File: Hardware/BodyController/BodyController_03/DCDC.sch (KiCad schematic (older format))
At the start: 58 parts, among them Q12 BUK9Y3R0-40E,115, Q13 BUK9Y3R0-40E,115, Q14 BUK9Y3R0-40E,115, Q16 2N7002, Q6 NX1029X,115, Q7 NX1029X,115, U21 LM2903QDRQ1, U25 UCC27511A-Q1, U27 INA21x, U28 OPA320-Q1

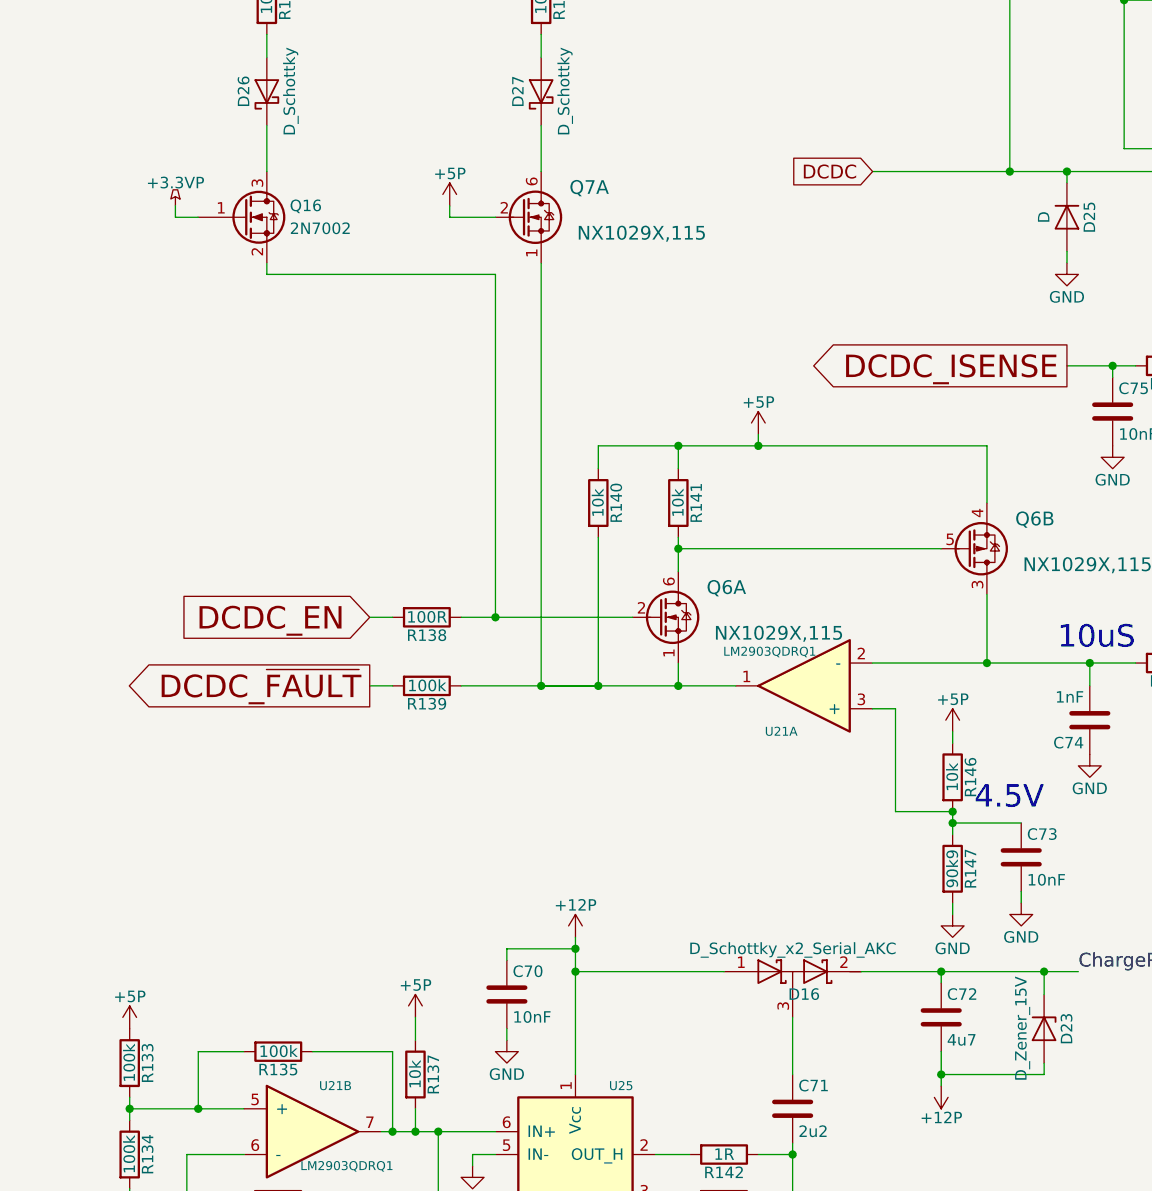
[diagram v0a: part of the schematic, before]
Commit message: Updated layout, cleaned up directory, and modified BOM
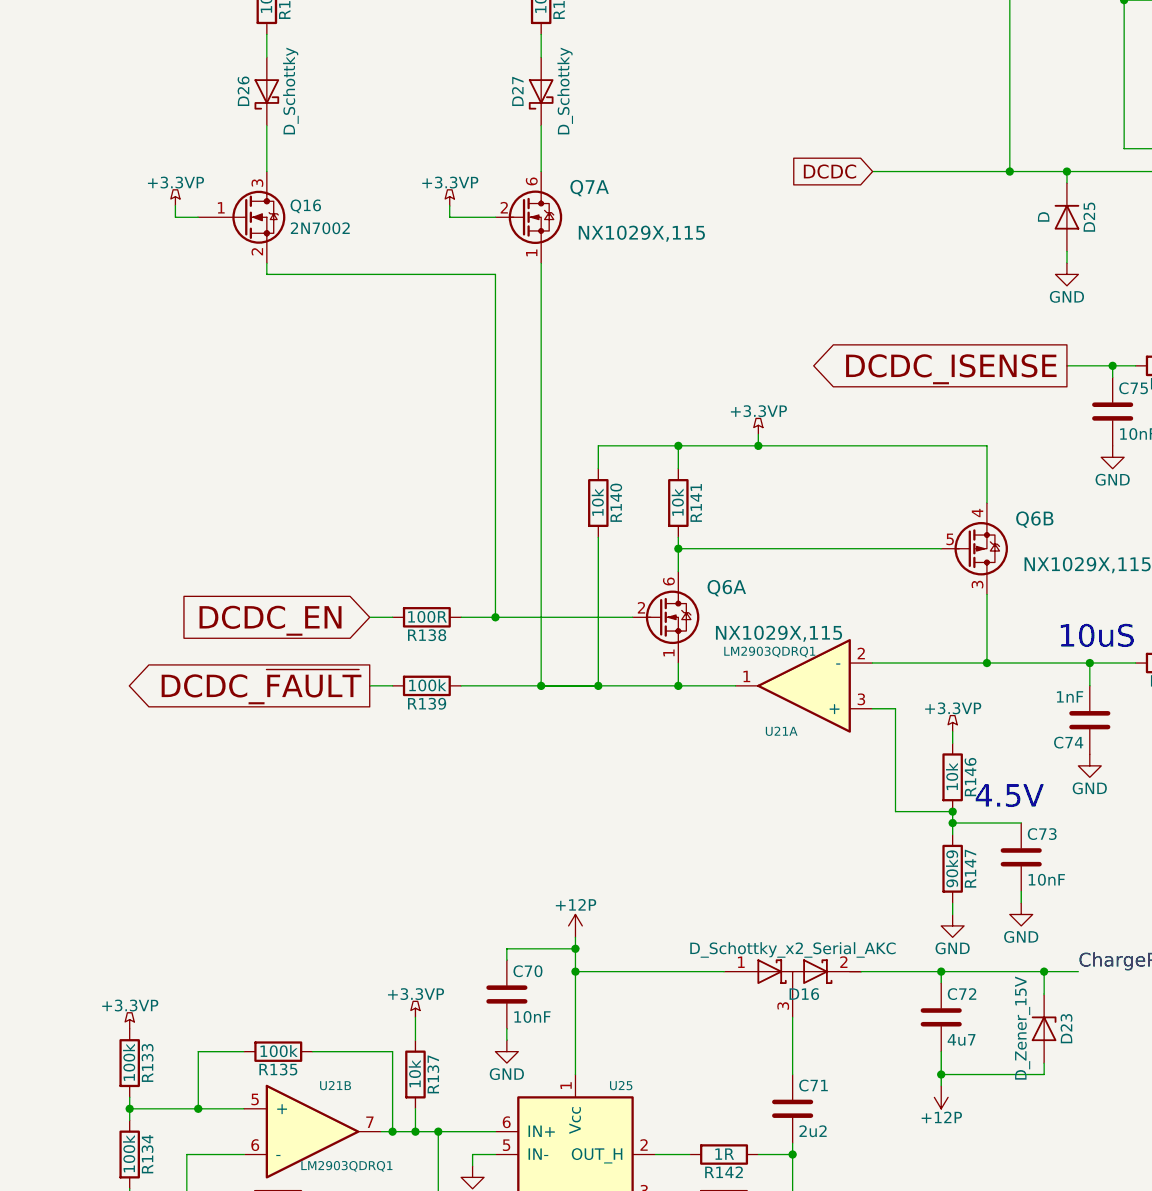
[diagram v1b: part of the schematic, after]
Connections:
- net +5P is gone; now on net +3.3VP: Q6.4, Q7.2, R133.1, R137.1, R140.1, R141.1, R146.1
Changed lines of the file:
@@
 EESchema Schematic File Version 2
+LIBS:BodyController_03-rescue
 LIBS:power
 LIBS:device
@@
 LIBS:contrib
 LIBS:valves
-LIBS:HSD
-LIBS:micros
-LIBS:ICs
-LIBS:Connectors
 LIBS:BodyController_03-cache
 EELAYER 25 0
@@
 $EndComp
 $Comp
-L +5P #PWR0163
-U 1 1 59A60638
-P 3300 3750
-F 0 "#PWR0163" H 3300 3600 50  0001 C CNN
-F 1 "+5P" H 3300 3890 50  0000 C CNN
-F 2 "" H 3300 3750 50  0001 C CNN
-F 3 "" H 3300 3750 50  0001 C CNN
-	1    3300 3750
-	1    0    0    -1
-$EndComp
-$Comp
 L R R140
 U 1 1 59A60639
@@
 F 3 "" H 2600 4050 50  0001 C CNN
 	1    2600 4050
-	1    0    0    -1
-$EndComp
-$Comp
-L +5P #PWR0164
-U 1 1 59A6063A
-P 4150 5050
-F 0 "#PWR0164" H 4150 4900 50  0001 C CNN
-F 1 "+5P" H 4150 5190 50  0000 C CNN
-F 2 "" H 4150 5050 50  0001 C CNN
-F 3 "" H 4150 5050 50  0001 C CNN
-	1    4150 5050
 	1    0    0    -1
 $EndComp
@@
 F 3 "" H 2350 1300 50  0001 C CNN
 	1    2350 1300
-	1    0    0    -1
-$EndComp
-$Comp
-L +5P #PWR0165
-U 1 1 59A60641
-P 1950 2750
-F 0 "#PWR0165" H 1950 2600 50  0001 C CNN
-F 1 "+5P" H 1950 2890 50  0000 C CNN
-F 2 "" H 1950 2750 50  0001 C CNN
-F 3 "" H 1950 2750 50  0001 C CNN
-	1    1950 2750
 	1    0    0    -1
 $EndComp
@@
 $EndComp
 $Comp
-L +12P #PWR0166
+L +12P #PWR0163
 U 1 1 59A60645
 P 2500 5950
-F 0 "#PWR0166" H 2500 5800 50  0001 C CNN
+F 0 "#PWR0163" H 2500 5800 50  0001 C CNN
 F 1 "+12P" H 2500 6090 50  0000 C CNN
 F 2 "" H 2500 5950 50  0001 C CNN
@@
 $EndComp
 $Comp
-L GND #PWR0167
+L GND #PWR0164
 U 1 1 59A6064B
 P 2200 6400
-F 0 "#PWR0167" H 2200 6150 50  0001 C CNN
+F 0 "#PWR0164" H 2200 6150 50  0001 C CNN
 F 1 "GND" H 2200 6250 50  0000 C CNN
 F 2 "" H 2200 6400 50  0001 C CNN
@@
 $EndComp
 $Comp
-L +12P #PWR0168
+L +12P #PWR0165
 U 1 1 59A6064C
 P 4100 6600
-F 0 "#PWR0168" H 4100 6450 50  0001 C CNN
+F 0 "#PWR0165" H 4100 6450 50  0001 C CNN
 F 1 "+12P" H 4100 6740 50  0000 C CNN
 F 2 "" H 4100 6600 50  0001 C CNN
@@
 $EndComp
 $Comp
-L GND #PWR0169
+L GND #PWR0166
 U 1 1 59A6064D
 P 2050 7300
-F 0 "#PWR0169" H 2050 7050 50  0001 C CNN
+F 0 "#PWR0166" H 2050 7050 50  0001 C CNN
 F 1 "GND" H 2050 7150 50  0000 C CNN
 F 2 "" H 2050 7300 50  0001 C CNN
@@
 $EndComp
 $Comp
-L GND #PWR0170
+L GND #PWR0167
 U 1 1 59A6064F
 P 2050 6950
-F 0 "#PWR0170" H 2050 6700 50  0001 C CNN
+F 0 "#PWR0167" H 2050 6700 50  0001 C CNN
 F 1 "GND" H 2050 6800 50  0000 C CNN
 F 2 "" H 2050 6950 50  0001 C CNN
@@
 F 3 "" H 1800 6550 50  0001 C CNN
 	1    1800 6550
-	1    0    0    -1
-$EndComp
-$Comp
-L +5P #PWR0171
-U 1 1 59A60651
-P 1800 6300
-F 0 "#PWR0171" H 1800 6150 50  0001 C CNN
-F 1 "+5P" H 1800 6440 50  0000 C CNN
-F 2 "" H 1800 6300 50  0001 C CNN
-F 3 "" H 1800 6300 50  0001 C CNN
-	1    1800 6300
 	1    0    0    -1
 $EndComp
@@
 $EndComp
 $Comp
-L GND #PWR0172
+L GND #PWR0168
 U 1 1 59A60654
 P 550 7100
-F 0 "#PWR0172" H 550 6850 50  0001 C CNN
+F 0 "#PWR0168" H 550 6850 50  0001 C CNN
 F 1 "GND" H 550 6950 50  0000 C CNN
 F 2 "" H 550 7100 50  0001 C CNN
@@
 $EndComp
 $Comp
-L GND #PWR0173
+L GND #PWR0169
 U 1 1 59A60656
 P 800 7500
-F 0 "#PWR0173" H 800 7250 50  0001 C CNN
+F 0 "#PWR0169" H 800 7250 50  0001 C CNN
 F 1 "GND" H 800 7350 50  0000 C CNN
 F 2 "" H 800 7500 50  0001 C CNN
@@
 F 3 "" H 550 6500 50  0001 C CNN
 	1    550  6500
-	1    0    0    -1
-$EndComp
-$Comp
-L +5P #PWR0174
-U 1 1 59A60658
-P 550 6350
-F 0 "#PWR0174" H 550 6200 50  0001 C CNN
-F 1 "+5P" H 550 6490 50  0000 C CNN
-F 2 "" H 550 6350 50  0001 C CNN
-F 3 "" H 550 6350 50  0001 C CNN
-	1    550  6350
 	1    0    0    -1
 $EndComp
@@
 $EndComp
 $Comp
-L GND #PWR0175
+L GND #PWR0170
 U 1 1 59B7AA18
 P 4650 3000
-F 0 "#PWR0175" H 4650 2750 50  0001 C CNN
+F 0 "#PWR0170" H 4650 2750 50  0001 C CNN
 F 1 "GND" H 4650 2850 50  0000 C CNN
 F 2 "" H 4650 3000 50  0001 C CNN
@@
 $EndComp
 $Comp
-L +3.3VP #PWR0176
+L +3.3VP #PWR0171
 U 1 1 59E68E49
 P 750 2750
-F 0 "#PWR0176" H 900 2700 50  0001 C CNN
+F 0 "#PWR0171" H 900 2700 50  0001 C CNN
 F 1 "+3.3VP" H 750 2850 50  0000 C CNN
 F 2 "" H 750 2750 50  0001 C CNN
@@
 Connection ~ 2100 1550
 Connection ~ 2150 4550
+$Comp
+L +3.3VP #PWR0172
+U 1 1 59ECEAE9
+P 1950 2750
+F 0 "#PWR0172" H 2100 2700 50  0001 C CNN
+F 1 "+3.3VP" H 1950 2850 50  0000 C CNN
+F 2 "" H 1950 2750 50  0001 C CNN
+F 3 "" H 1950 2750 50  0001 C CNN
+	1    1950 2750
+	1    0    0    -1
+$EndComp
+$Comp
+L +3.3VP #PWR0173
+U 1 1 59ECEBB4
+P 3300 3750
+F 0 "#PWR0173" H 3450 3700 50  0001 C CNN
+F 1 "+3.3VP" H 3300 3850 50  0000 C CNN
+F 2 "" H 3300 3750 50  0001 C CNN
+F 3 "" H 3300 3750 50  0001 C CNN
+	1    3300 3750
+	1    0    0    -1
+$EndComp
+$Comp
+L +3.3VP #PWR0174
+U 1 1 59ECEDFF
+P 1800 6300
+F 0 "#PWR0174" H 1950 6250 50  0001 C CNN
+F 1 "+3.3VP" H 1800 6400 50  0000 C CNN
+F 2 "" H 1800 6300 50  0001 C CNN
+F 3 "" H 1800 6300 50  0001 C CNN
+	1    1800 6300
+	1    0    0    -1
+$EndComp
+$Comp
+L +3.3VP #PWR0175
+U 1 1 59ECF0CA
+P 550 6350
+F 0 "#PWR0175" H 700 6300 50  0001 C CNN
+F 1 "+3.3VP" H 550 6450 50  0000 C CNN
+F 2 "" H 550 6350 50  0001 C CNN
+F 3 "" H 550 6350 50  0001 C CNN
+	1    550  6350
+	1    0    0    -1
+$EndComp
+$Comp
+L +3.3VP #PWR0176
+U 1 1 59ECFE5D
+P 4150 5050
+F 0 "#PWR0176" H 4300 5000 50  0001 C CNN
+F 1 "+3.3VP" H 4150 5150 50  0000 C CNN
+F 2 "" H 4150 5050 50  0001 C CNN
+F 3 "" H 4150 5050 50  0001 C CNN
+	1    4150 5050
+	1    0    0    -1
+$EndComp
 $EndSCHEMATC

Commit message: started serious layout
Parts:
- removed C82: 10nF, Capacitors_SMD:C_0603, symbol C
- removed Q14: BUK9Y3R0-40E,115, TO_SOT_Packages_SMD:TDSON-8-1, symbol BUK9Y3R0-40E,115
- removed R151: 3R, Resistors_SMD:R_0603, symbol R
- removed R156: 0m4, Footprints:PSR500, symbol R_Shunt
- removed U28: OPA320-Q1, TO_SOT_Packages_SMD:SOT-23-5, symbol OPA320-Q1
- added C57: 1nF, Capacitors_SMD:C_0603, symbol C
- added R156: R0005, Resistors_SMD:R_2512, symbol R
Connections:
- net +12V: now also R154.1, R156.1
- net GND: now also C57.1
- net at R155.1: now also Q12.5 (D), Q13.5 (D), R156.2
- net at C79.1, R157.2, R158.1: now also U27.1 (REF)
- net at Q6.1, Q7.1, R139.1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: now also C57.2
- net DCDC_ISENSE renamed DCDC_ISENSE_AI
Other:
- moved on the sheet: C79, R157, R158

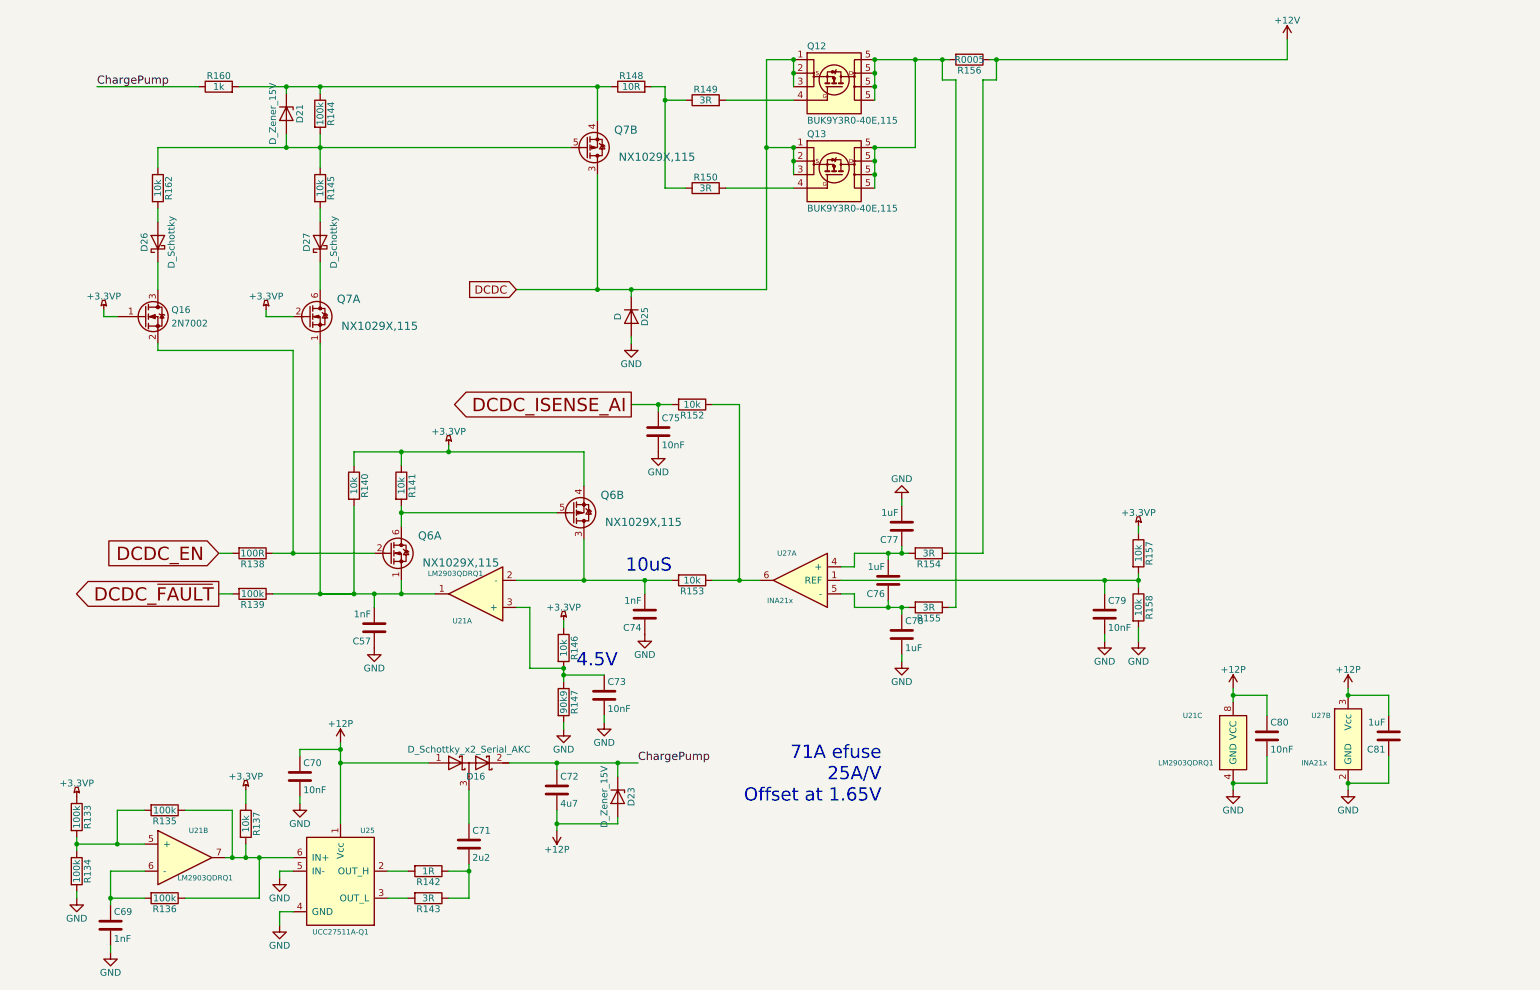
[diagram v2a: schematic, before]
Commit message: Body Controller Layout Done
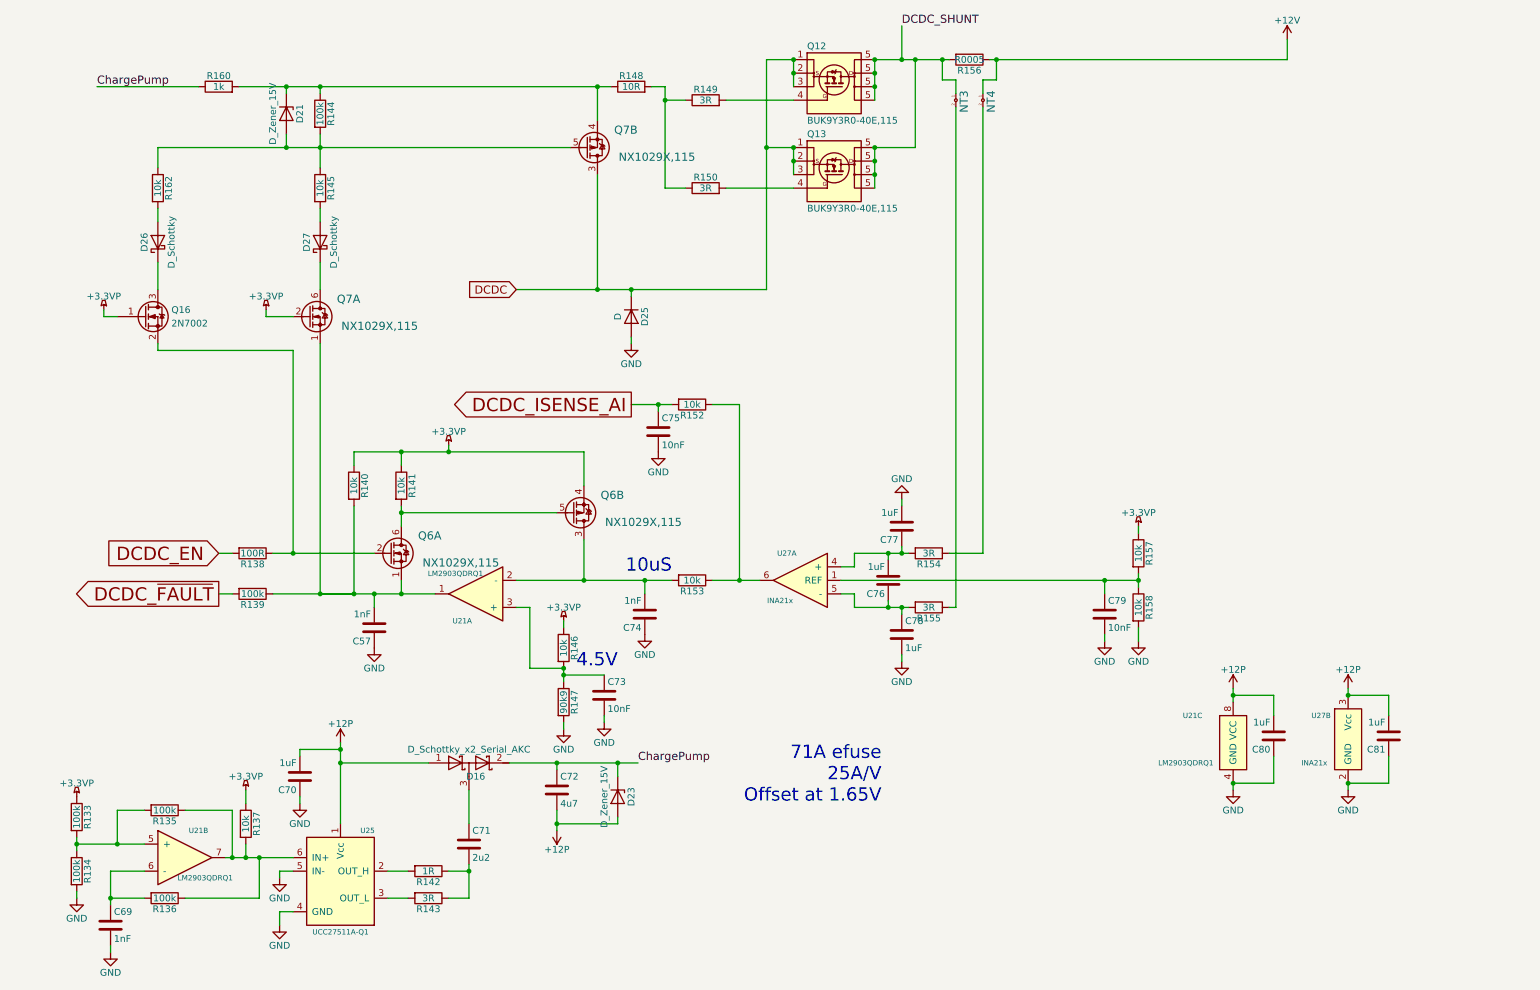
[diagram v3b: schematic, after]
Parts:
- added NT3, NT4: Net_Tie-0.5mm, Footprints:Net_Tie-0.5mm, symbol Net_Tie-0.5mm
- C70, C80: value 10nF -> 1uF; footprint Capacitors_SMD:C_0603 -> Capacitors_SMD:C_0805; PartNumber CGA3E2X7R1H103K080AA -> CGA4J3X7R1H105K125AE
- D25: footprint Diodes_SMD:D_SMB -> Footprints:SOT1289; PartNumber S3AB -> PMEG060V100EPDZ
- R156: footprint Resistors_SMD:R_2512 -> SMD_Packages:SMD-2512_Pol
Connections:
- net +12P: now also C70.2, C80.2; no longer C70.1, C80.1
- net +12V: now also NT4.1; no longer R154.1
- net GND: now also C70.1, C80.1; no longer C70.2, C80.2
- net DCDC_SHUNT: now reaches Q12.5 (D), Q13.5 (D), R156.2
- net DCDC_SHUNT: now also NT3.1; no longer R155.1
- new net: NT4.2, R154.1
- new net: NT3.2, R155.1
